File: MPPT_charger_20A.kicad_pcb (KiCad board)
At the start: 2 copper layers, 114.5 x 60.5 mm, 151 parts, among them J1 SOLAR, J2 LOAD, J3 BAT, J4 UEXT, J5 CONN_01X03, P1 CONN_01X02, P3 USB Micro B, Q1 CSD18540Q5B, Q2 CSD18540Q5B, Q3 CSD18540Q5B, Q4 CSD18540Q5B, Q5 BSS84, Q6 BSS84, Q7 BSS84, SW1 SW_PUSH, T1 MMBT3904, T2 MMBT3904, T3 MMBT3904, T4 MMBT3904, U1 LM5107, U2 STM32F072CB, U3 AZ1117, U4 LMR16006X, U5 AP2210-3.3, U6 24AA01, U7 LM258, U8 TJA1042T/3, Y1 8MHz

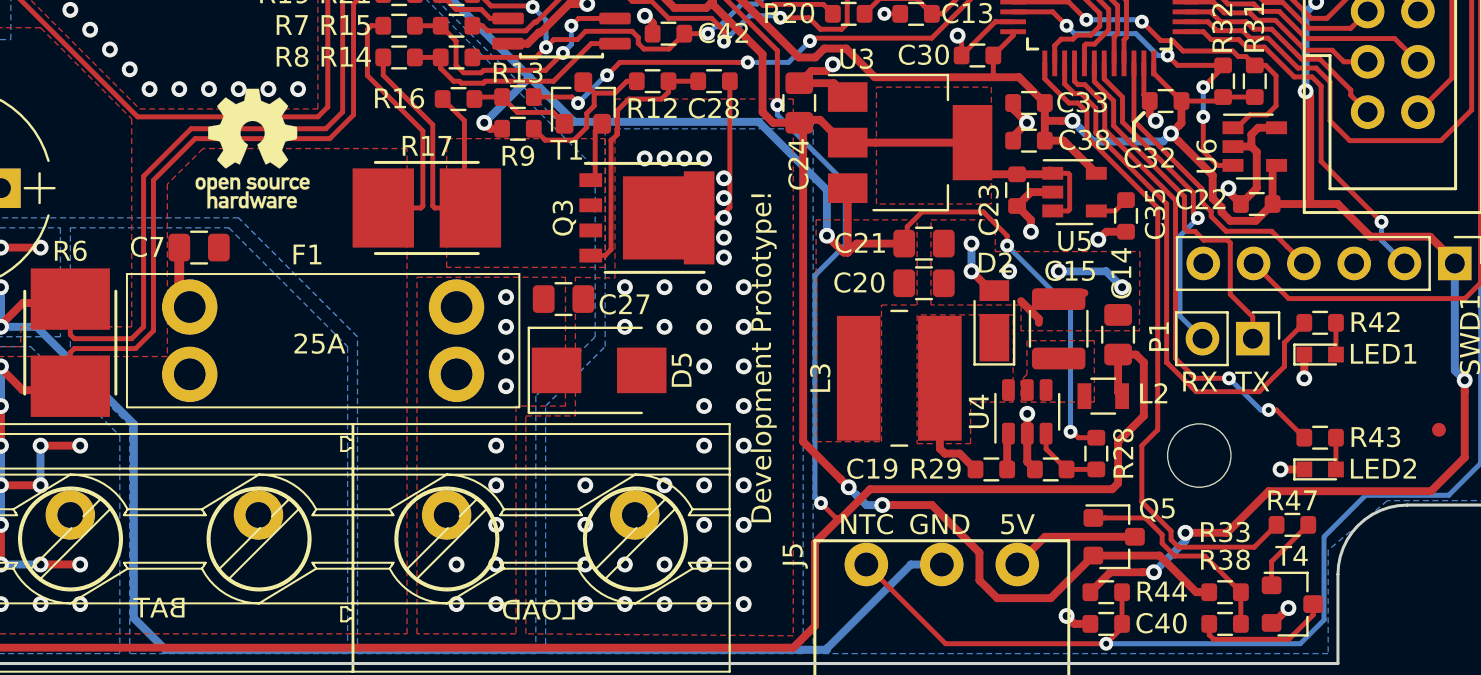
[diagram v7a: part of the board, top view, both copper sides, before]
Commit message: Adjustments to use MP2459 as SMPS (previous one out of stock)
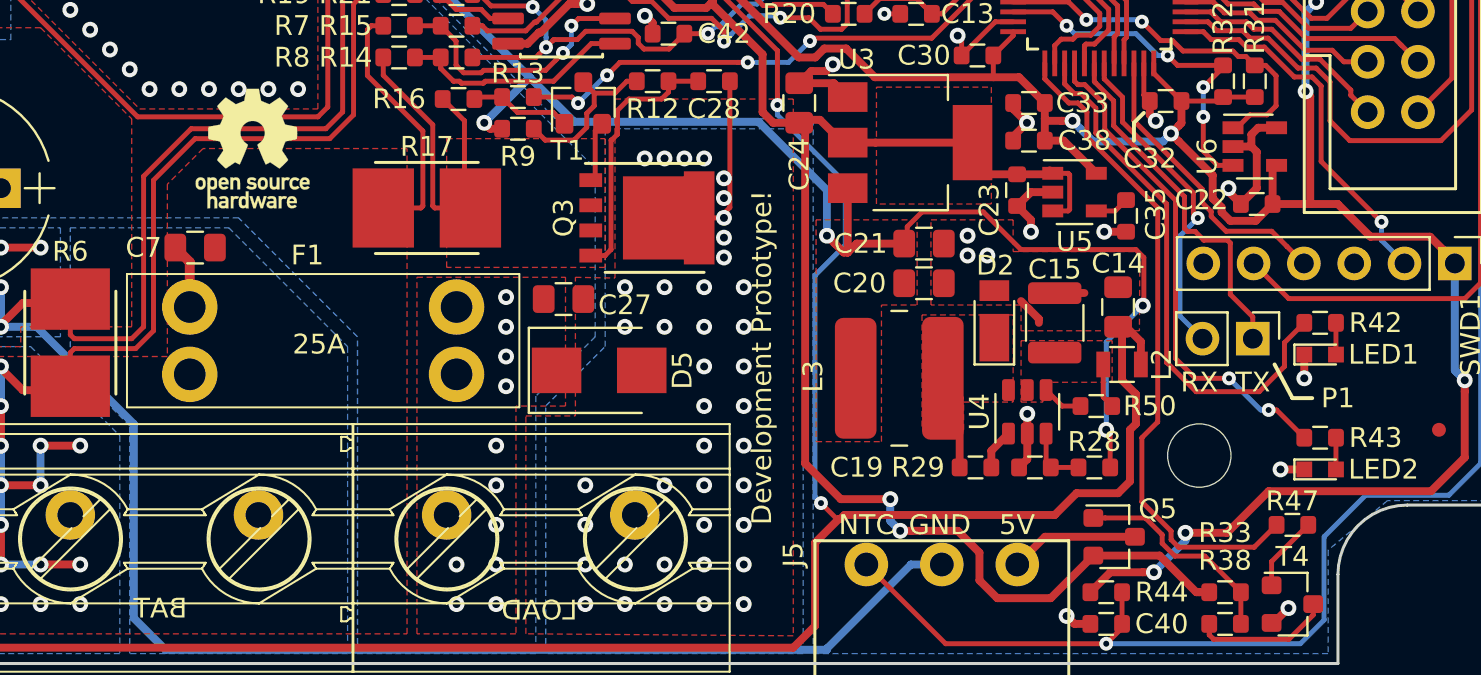
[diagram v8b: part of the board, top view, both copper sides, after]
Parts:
- added R50: 1M, LibreSolar:R_0603_1608, F.Cu at (192.8, 125.0)
- L3: footprint LibreSolar:L_Wuerth_WE-TPC-58xx -> LibreSolar:Bourns_SRN6045TA
- R28: value 120k -> 110k
- U4: value LMR16006X -> MP2459
- moved L2 1.86 mm to (194.1, 122.9)
- moved C14 1.40 mm to (193.9, 120.0)
- moved C19 0.81 mm to (186.7, 128.1)
- moved R29 0.81 mm to (189.7, 128.1)
- moved R28 0.71 mm to (192.7, 128.1), turned to 180 degrees
- moved C15 0.36 mm to (190.7, 120.8)
- moved C7 0.20 mm to (147.3, 117.0)
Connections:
- U4 pad 4: Net-(C15-Pad1) -> Net-(R50-Pad1)
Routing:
- net GND: track 343.4 -> 336.5 mm, vias 116 -> 114
- net +10V: track 106.3 -> 112.4 mm
- net Net-(C15-Pad1): track 0.00 -> 2.29 mm
- net Net-(R50-Pad1): track 0.00 -> 2.07 mm
- net /DCDC power stage/DCDC_IN: track 157.2 -> 158.4 mm
- net +5V: track 174.6 -> 175.8 mm
- net Net-(C19-Pad1): track 1.83 -> 2.40 mm
- net Net-(R28-Pad2): track 3.74 -> 3.20 mm
